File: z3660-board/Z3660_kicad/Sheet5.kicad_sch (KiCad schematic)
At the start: 57 parts, among them CN2 Conn_02x40_Odd_Even, CN3 Conn_02x40_Odd_Even, U1 LTC2990, U15 SN74CB3T3245PW, U16 SN74CB3T3245PW, U17 SN74CB3T3245PW, U18 SN74CB3T3245PW

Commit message: Update to version v0.21a
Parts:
- C41: footprint Z3660_v02:C_Elec_5x5.4 -> Z3660_v02:CP_Elec_6.3x3.9
- NT3: footprint NetTie:NetTie-2_SMD_Pad0.5mm -> Z3660_v02:NetTie-2_SMD_Pad0.5mm

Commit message: Update led values values to differentiate green and red.
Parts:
- D1: value LED_Small -> LED_Small_Green
- D2: value LED_Small -> LED_Small_Red
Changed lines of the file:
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@@
       (effects (font (size 1.27 1.27)) (justify right))
     )
-    (property "Value" "LED_Small" (at 257.048 72.263 90)
+    (property "Value" "LED_Small_Green" (at 247.65 60.96 90)
       (effects (font (size 1.27 1.27)) (justify right))
     )
@@
       (effects (font (size 1.27 1.27)) (justify right))
     )
-    (property "Value" "LED_Small" (at 272.288 72.263 90)
+    (property "Value" "LED_Small_Red" (at 269.24 60.96 90)
       (effects (font (size 1.27 1.27)) (justify right))
     )

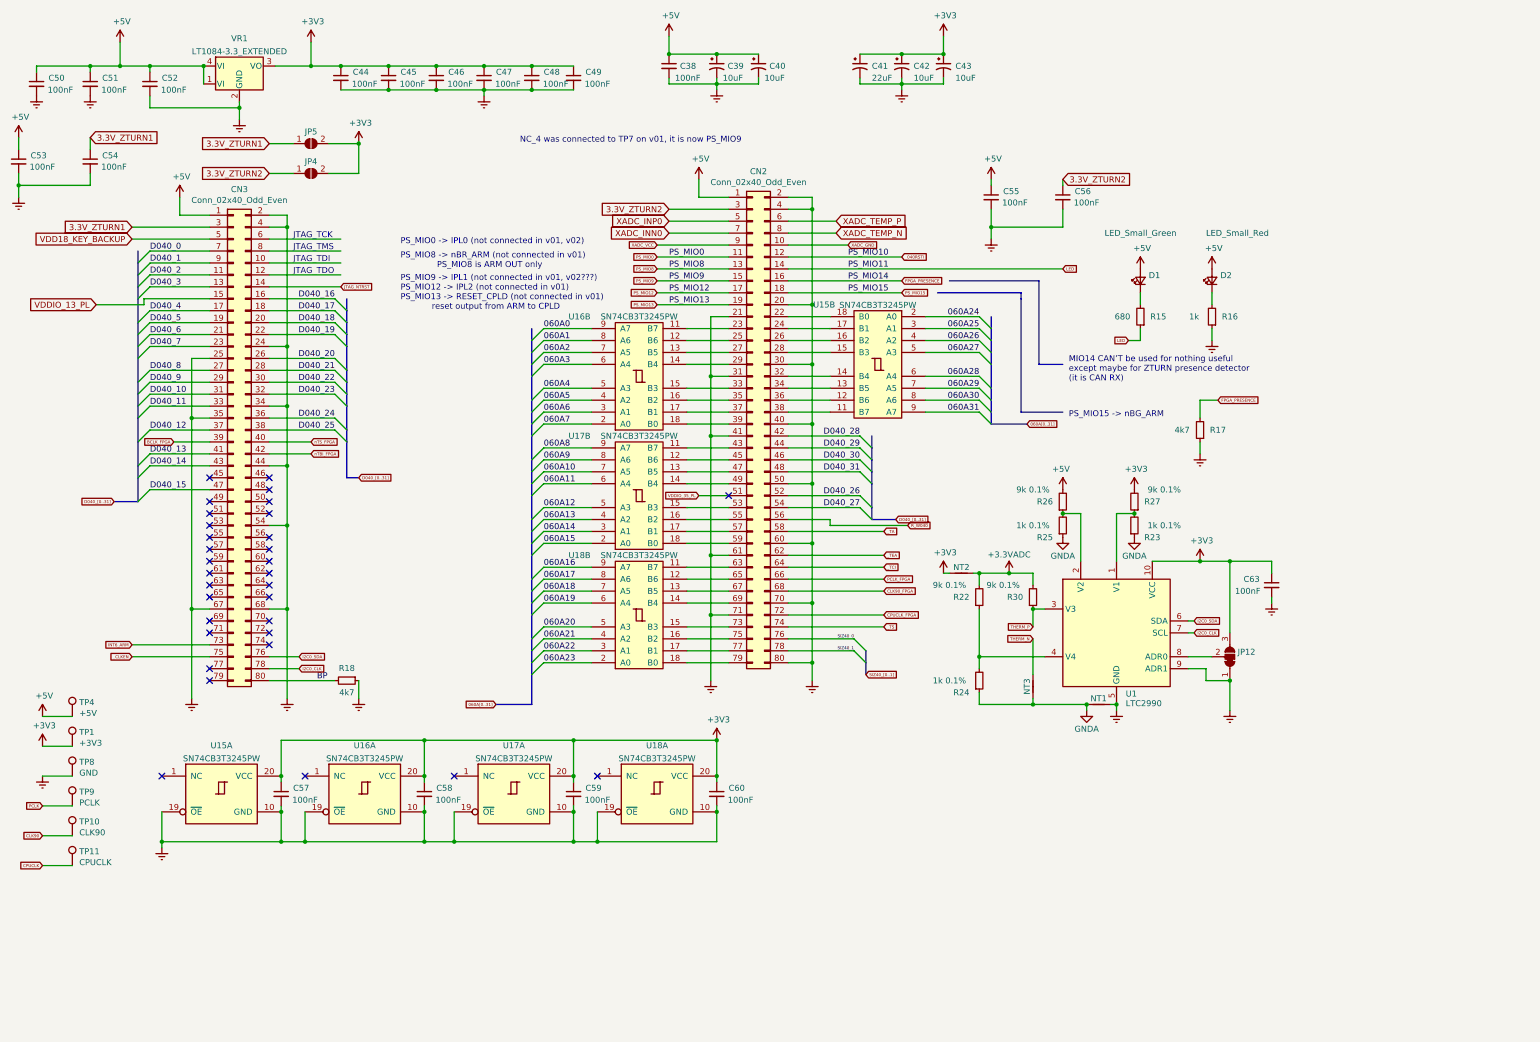
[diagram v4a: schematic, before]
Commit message: Hardware version v.022 adds CPLD programmer. Also a tiny PCB for v.021x
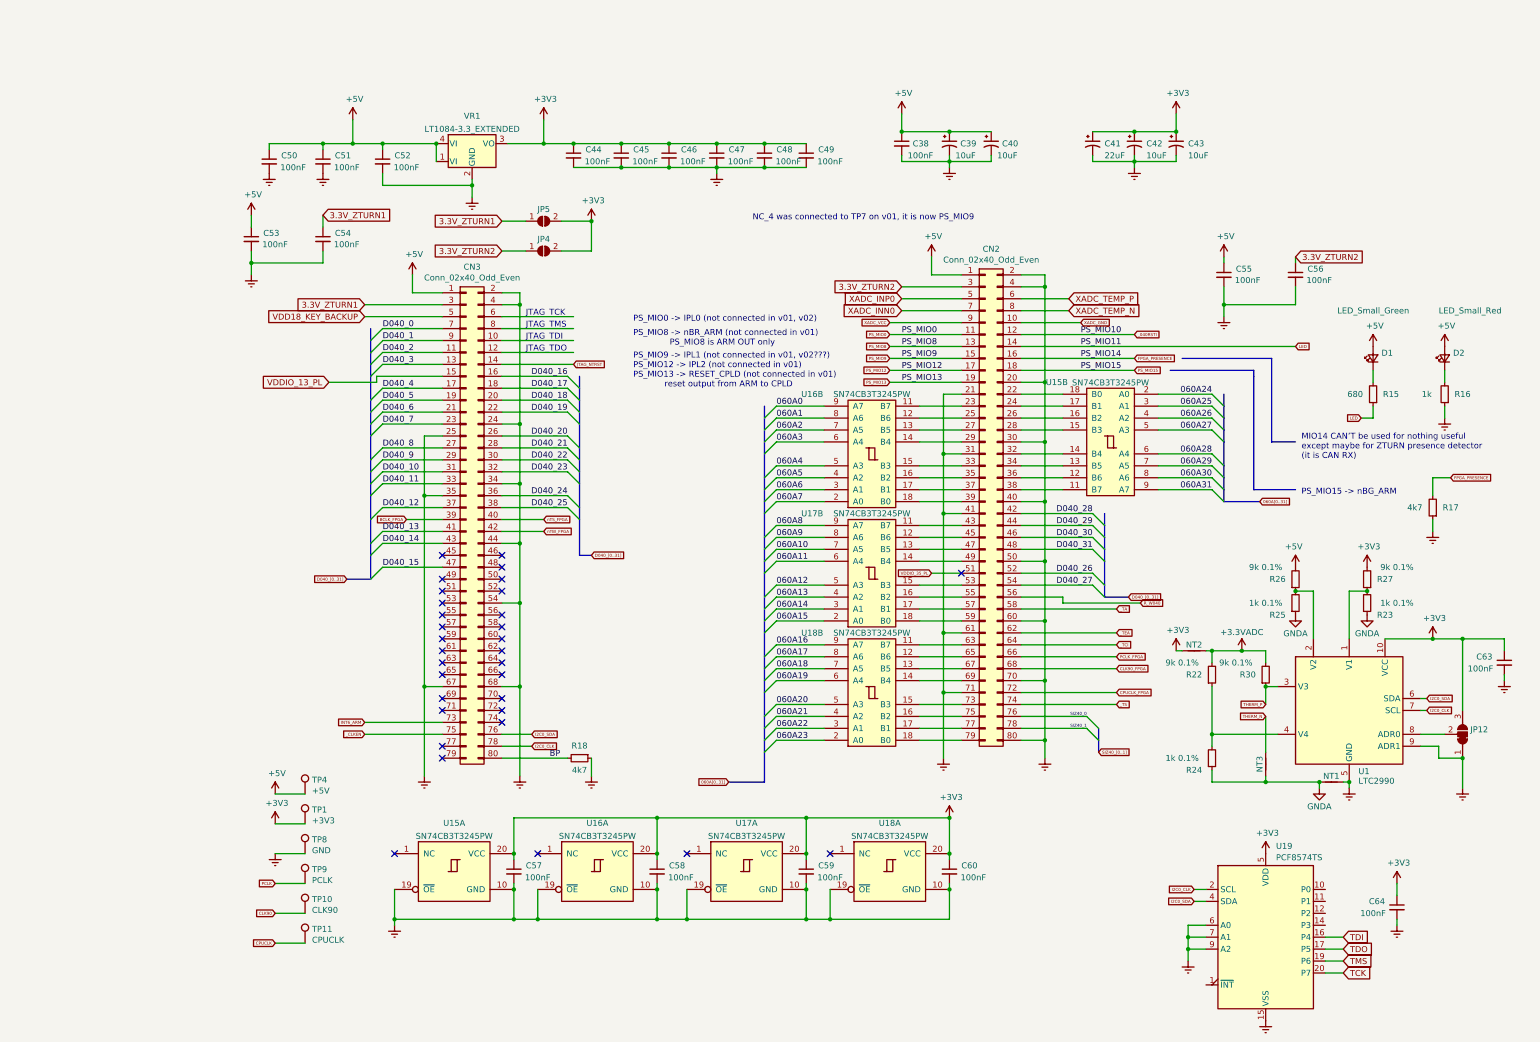
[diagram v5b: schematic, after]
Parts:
- added C64: 100nF, Z3660_v02:C_0805_2012Metric_Pad1.18x1.45mm_HandSolder, symbol Z3660_v02:C_Small
- added U19: PCF8574TS, Z3660_v02:SSOP-20_4.4x6.5mm_P0.65mm, symbol Interface_Expansion:PCF8574TS
- CN3: footprint Z3660_v02:PinHeader_2x40_P1.27mm_Vertical -> Z3660_v02:PinHeader_2x40_P1.27mm_Vertical_CN3
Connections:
- net +3V3: now also C64.1, U19.5 (VDD)
- net Earth: now also C64.2, U19.15 (VSS), U19.6 (A0), U19.7 (A1), U19.9 (A2)
- net I2C0_CLK: now also U19.2 (SCL)
- net I2C0_SDA: now also U19.4 (SDA)
- new net TCK: U19.20 (P7)
- new net TDI: U19.16 (P4)
- new net TDO: U19.17 (P5)
- new net TMS: U19.19 (P6)
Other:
- moved on the sheet: C38, C39, C40, C41, C42, C43, C44, C45, C46, C47, C48, C49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
